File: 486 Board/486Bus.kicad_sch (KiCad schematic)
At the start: 16 parts, among them J1 PWR, J10 Cache, J11 Not Connected, J12 Parity, J13 FPU, J14 PWR, J15 PWR, J2 Address Bus, J3 Data Bus, J4 Control Bus, J5 Control Lines, J6 Input, J7 Byte Enabled, J8 Bus Size, J9 Bus Arbitration

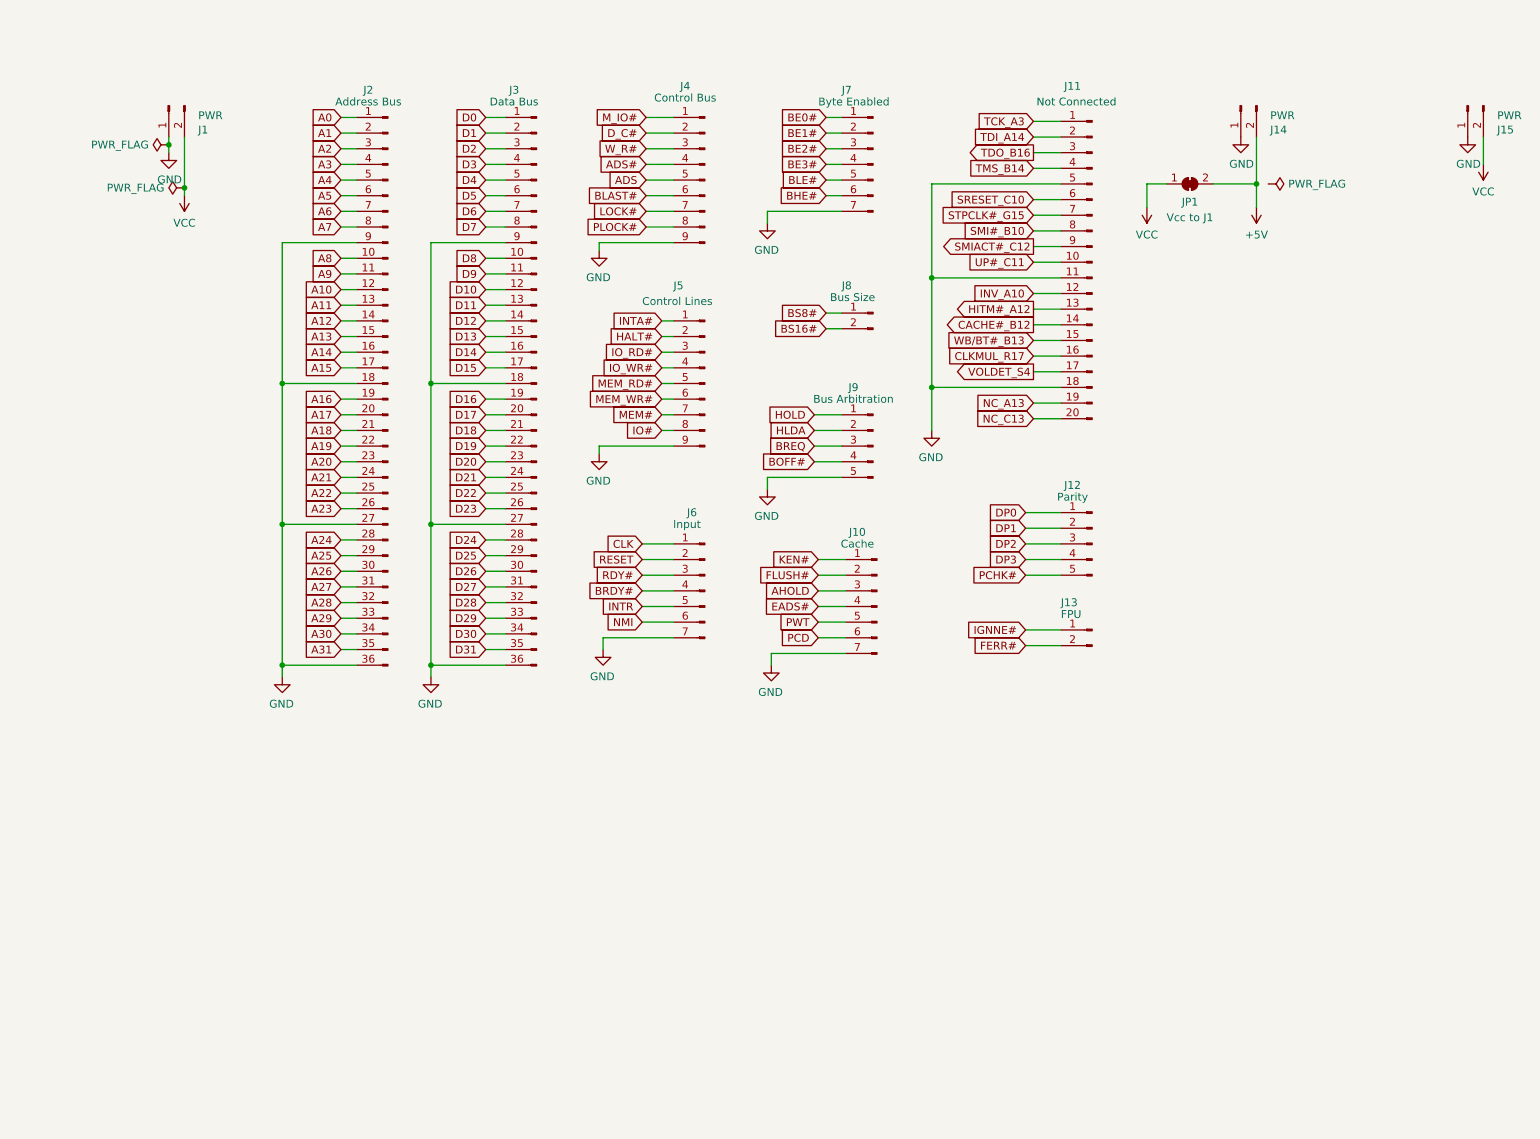
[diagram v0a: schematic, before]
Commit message: * Layout Template for eurocard format * 486 Board updated to new layout * Support board draft * Added 6u eurocard backplane meant for ATX case
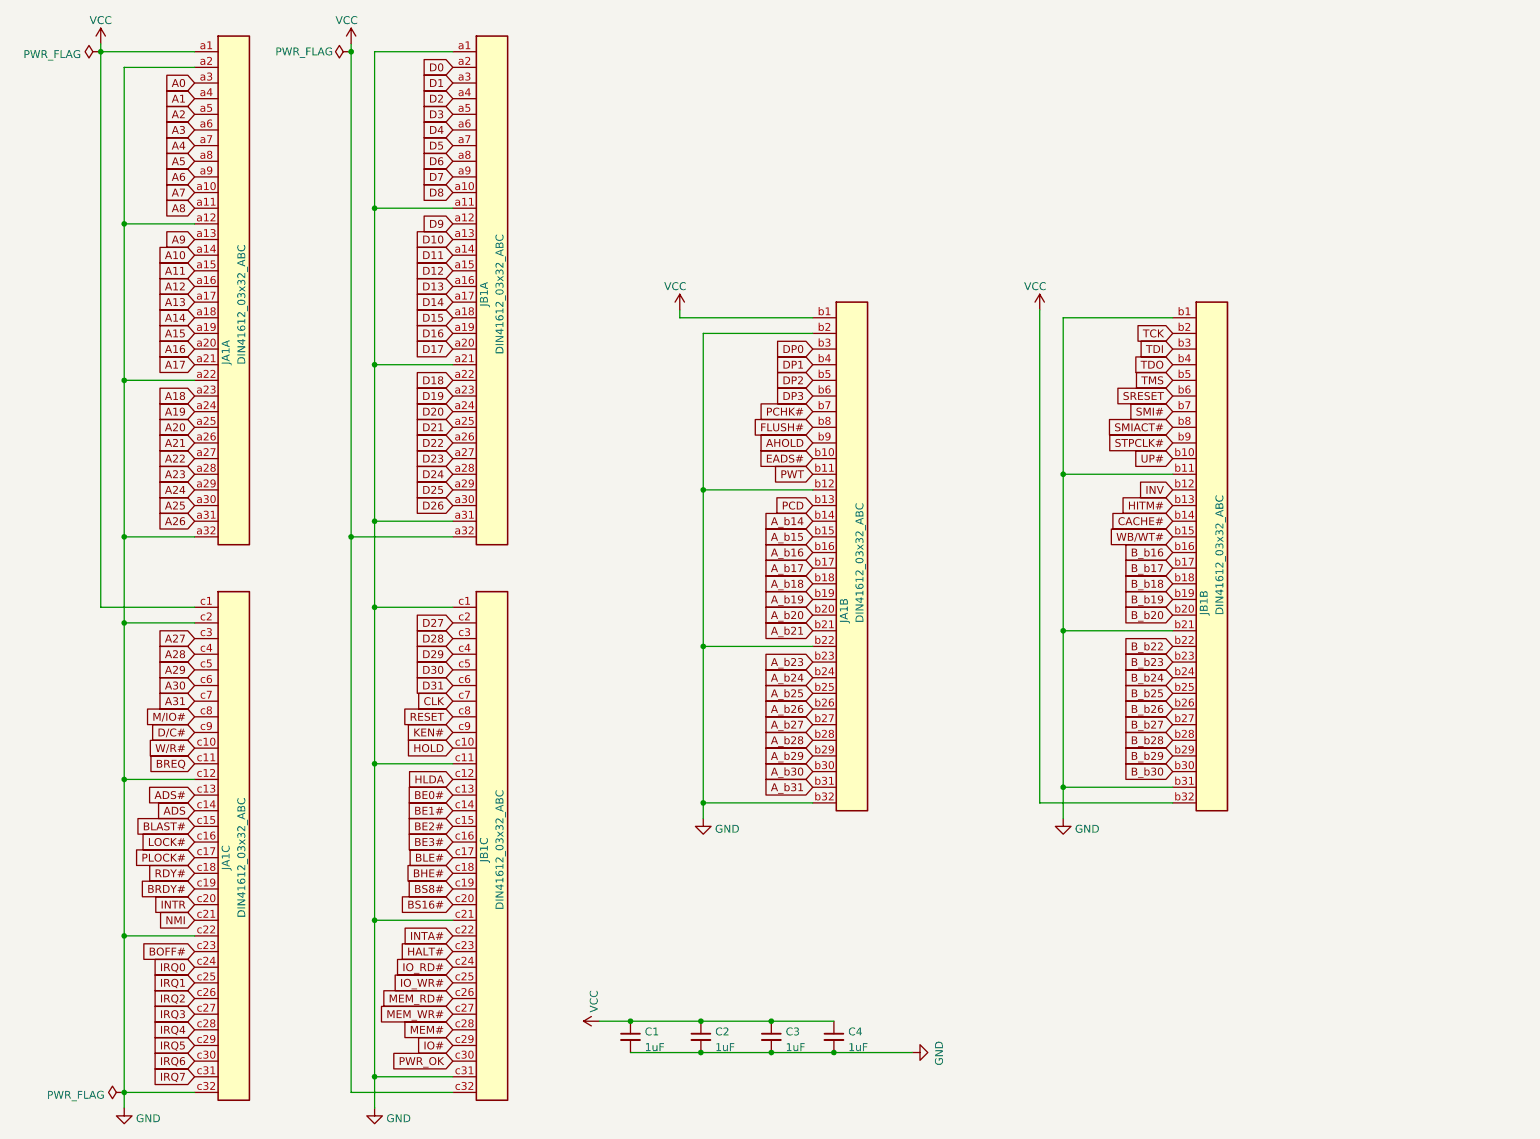
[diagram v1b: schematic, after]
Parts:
- removed J1, J14, J15: PWR, Connector_PinHeader_2.54mm:PinHeader_1x02_P2.54mm_Vertical, symbol Connector:Conn_01x02_Male
- removed J10: Cache, Connector_PinHeader_2.54mm:PinHeader_1x07_P2.54mm_Vertical, symbol Connector:Conn_01x07_Male
- removed J11: Not Connected, Connector_PinHeader_2.54mm:PinHeader_1x20_P2.54mm_Vertical, symbol Connector:Conn_01x20_Male
- removed J12: Parity, Connector_PinHeader_2.54mm:PinHeader_1x05_P2.54mm_Vertical, symbol Connector:Conn_01x05_Male
- removed J13: FPU, Connector_PinHeader_2.54mm:PinHeader_1x02_P2.54mm_Vertical, symbol Connector:Conn_01x02_Male
- removed J2: Address Bus, Connector_PinHeader_2.54mm:PinHeader_1x36_P2.54mm_Vertical, symbol Connector:Conn_01x36_Male
- removed J3: Data Bus, Connector_PinHeader_2.54mm:PinHeader_1x36_P2.54mm_Vertical, symbol Connector:Conn_01x36_Male
- removed J4: Control Bus, Connector_PinHeader_2.54mm:PinHeader_1x09_P2.54mm_Vertical, symbol Connector:Conn_01x09_Male
- removed J5: Control Lines, Connector_PinHeader_2.54mm:PinHeader_1x09_P2.54mm_Vertical, symbol Connector:Conn_01x09_Male
- removed J6: Input, Connector_PinHeader_2.54mm:PinHeader_1x07_P2.54mm_Vertical, symbol Connector:Conn_01x07_Male
- removed J7: Byte Enabled, Connector_PinHeader_2.54mm:PinHeader_1x07_P2.54mm_Vertical, symbol Connector:Conn_01x07_Male
- removed J8: Bus Size, Connector_PinHeader_2.54mm:PinHeader_1x02_P2.54mm_Vertical, symbol Connector:Conn_01x02_Male
- removed J9: Bus Arbitration, Connector_PinHeader_2.54mm:PinHeader_1x05_P2.54mm_Vertical, symbol Connector:Conn_01x05_Male
- removed JP1: Vcc to J1, Jumper:SolderJumper-2_P1.3mm_Bridged_Pad1.0x1.5mm, symbol Jumper:SolderJumper_2_Bridged
- added C1, C2, C3, C4: 1uF, Capacitor_SMD:C_0805_2012Metric_Pad1.18x1.45mm_HandSolder, symbol Device:C_Small
- added JA1, JB1: DIN41612_03x32_ABC, Connector_DIN:DIN41612_R_3x32_Male_Horizontal_THT, symbol Private Lib:DIN41612_03x32_ABC
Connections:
- net A0: now also JA1.a3
- net A1: now also JA1.a4
- net A10: now also JA1.a14
- net A11: now also JA1.a15
- net A12: now also JA1.a16
- net A13: now also JA1.a17
- net A14: now also JA1.a18
- net A15: now also JA1.a19
- net A16: now also JA1.a20
- net A17: now also JA1.a21
- net A18: now also JA1.a23
- net A19: now also JA1.a24
- net A2: now also JA1.a5
- net A20: now also JA1.a25
- net A21: now also JA1.a26
- net A22: now also JA1.a27
- net A23: now also JA1.a28
- net A24: now also JA1.a29
- net A25: now also JA1.a30
- net A26: now also JA1.a31
- net A27: now also JA1.c3
- net A28: now also JA1.c4
- net A29: now also JA1.c5
- net A3: now also JA1.a6
- net A30: now also JA1.c6
- net A31: now also JA1.c7
- net A4: now also JA1.a7
- net A5: now also JA1.a8
- net A6: now also JA1.a9
- net A7: now also JA1.a10
- net A8: now also JA1.a11
- net A9: now also JA1.a13
- net ADS: now also JA1.c14
- net ADS#: now also JA1.c13
- net AHOLD: now also JA1.b9
- net BE0#: now also JB1.c13
- net BE1#: now also JB1.c14
- net BE2#: now also JB1.c15
- net BE3#: now also JB1.c16
- net BHE#: now also JB1.c18
- net BLAST#: now also JA1.c15
- net BLE#: now also JB1.c17
- net BOFF#: now also JA1.c23
- net BRDY#: now also JA1.c19
- net BREQ: now also JA1.c11
- net BS16#: now also JB1.c20
- net BS8#: now also JB1.c19
- net CLK: now also JB1.c7
- net D0: now also JB1.a2
- net D1: now also JB1.a3
- net D10: now also JB1.a13
- net D11: now also JB1.a14
- net D12: now also JB1.a15
- net D13: now also JB1.a16
- net D14: now also JB1.a17
- net D15: now also JB1.a18
- net D16: now also JB1.a19
- net D17: now also JB1.a20
- net D18: now also JB1.a22
- net D19: now also JB1.a23
- net D2: now also JB1.a4
- net D20: now also JB1.a24
- net D21: now also JB1.a25
- net D22: now also JB1.a26
- net D23: now also JB1.a27
- net D24: now also JB1.a28
- net D25: now also JB1.a29
- net D26: now also JB1.a30
- net D27: now also JB1.c2
- net D28: now also JB1.c3
- net D29: now also JB1.c4
- net D3: now also JB1.a5
- net D30: now also JB1.c5
- net D31: now also JB1.c6
- net D4: now also JB1.a6
- net D5: now also JB1.a7
- net D6: now also JB1.a8
- net D7: now also JB1.a9
- net D8: now also JB1.a10
- net D9: now also JB1.a12
- net DP0: now also JA1.b3
- net DP1: now also JA1.b4
- net DP2: now also JA1.b5
- net DP3: now also JA1.b6
- net EADS#: now also JA1.b10
- net FLUSH#: now also JA1.b8
- net GND: now also C1.2, C2.2, C3.2, C4.2, JA1.a12, JA1.a2, JA1.a22, JA1.a32, JA1.b12, JA1.b2, JA1.b22, JA1.b32, JA1.c12, JA1.c2, JA1.c22, JA1.c32, JB1.a1, JB1.a11, JB1.a21, JB1.a31, JB1.b1, JB1.b11, JB1.b21, JB1.b31, JB1.c1, JB1.c11, JB1.c21, JB1.c31
- net HALT#: now also JB1.c23
- net HLDA: now also JB1.c12
- net HOLD: now also JB1.c10
- net INTA#: now also JB1.c22
- net INTR: now also JA1.c20
- net IO#: now also JB1.c29
- net IO_RD#: now also JB1.c24
- net IO_WR#: now also JB1.c25
- net KEN#: now also JB1.c9
- net LOCK#: now also JA1.c16
- net MEM#: now also JB1.c28
- net MEM_RD#: now also JB1.c26
- net MEM_WR#: now also JB1.c27
- net NMI: now also JA1.c21
- net PCD: now also JA1.b13
- net PCHK#: now also JA1.b7
- net PLOCK#: now also JA1.c17
- net PWT: now also JA1.b11
- net RDY#: now also JA1.c18
- net RESET: now also JB1.c8
- net VCC: now also C1.1, C2.1, C3.1, C4.1, JA1.a1, JA1.b1, JA1.c1, JB1.a32, JB1.b32, JB1.c32
- new net A_b14: JA1.b14
- new net A_b15: JA1.b15
- new net A_b16: JA1.b16
- new net A_b17: JA1.b17
- new net A_b18: JA1.b18
- new net A_b19: JA1.b19
- new net A_b20: JA1.b20
- new net A_b21: JA1.b21
- new net A_b23: JA1.b23
- new net A_b24: JA1.b24
- new net A_b25: JA1.b25
- new net A_b26: JA1.b26
- new net A_b27: JA1.b27
- new net A_b28: JA1.b28
- new net A_b29: JA1.b29
- new net A_b30: JA1.b30
- new net A_b31: JA1.b31
- new net B_b16: JB1.b16
- new net B_b17: JB1.b17
- new net B_b18: JB1.b18
- new net B_b19: JB1.b19
- new net B_b20: JB1.b20
- new net B_b22: JB1.b22
- new net B_b23: JB1.b23
- new net B_b24: JB1.b24
- new net B_b25: JB1.b25
- new net B_b26: JB1.b26
- new net B_b27: JB1.b27
- new net B_b28: JB1.b28
- new net B_b29: JB1.b29
- new net B_b30: JB1.b30
- new net CACHE#: JB1.b14
- new net D/C#: JA1.c9
- new net HITM#: JB1.b13
- new net INV: JB1.b12
- new net IRQ0: JA1.c24
- new net IRQ1: JA1.c25
- new net IRQ2: JA1.c26
- new net IRQ3: JA1.c27
- new net IRQ4: JA1.c28
- new net IRQ5: JA1.c29
- new net IRQ6: JA1.c30
- new net IRQ7: JA1.c31
- new net M/IO#: JA1.c8
- new net PWR_OK: JB1.c30
- new net SMI#: JB1.b7
- new net SMIACT#: JB1.b8
- new net SRESET: JB1.b6
- new net STPCLK#: JB1.b9
- new net TCK: JB1.b2
- new net TDI: JB1.b3
- new net TDO: JB1.b4
- new net TMS: JB1.b5
- new net UP#: JB1.b10
- new net WB/WT#: JB1.b15
- new net W/R#: JA1.c10
